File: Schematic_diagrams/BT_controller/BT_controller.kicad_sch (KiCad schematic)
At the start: 35 parts, among them J1 Conn_01x02_Socket, J1 Conn_2_Pin, J10 Conn_01x15_Socket, J11 Screw_Terminal_13-24_double_r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, J12 Screw_Terminal_58-60_double_r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, J13 Screw_Terminal_61-72_double_r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, J14 Screw_Terminal_3-4_partial_do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, J15 Conn_7_Pin, J2 D Sub Conn_9_Pin, J3 D Sub Conn_15_Pin, J4 Conn_01x07_Socket, J5 Conn_01x07_Socket, J5 Conn_7_Pin, J6 Screw_Terminal_13-24_double_r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, J7 Screw_Terminal_3-4_partial_do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, J8 Screw_Terminal_37-41_double_r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, J9 Screw_Terminal_1-2_partial_do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, SW1 ON/OFF, SW1 Start, SW3 SW_SPDT

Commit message: updates to rev B
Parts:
- added C2: 4700uF, symbol Device:C_Polarized
- added C3, C4: 0.1uF, symbol Device:C_Small
- added D2: SA12CA, symbol Device:D_TVS_Small_Filled
- added R2: 100R, symbol Device:R_Small
- BT_Bell_Push: value (none) -> SPST
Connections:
- net +10V: now also C2.1, C3.1, D2.2 (A2)
- net 8_Channel Relay Module #2/o/p8: now also R2.2
- net <- BT BELL SOUNDER (note 2): now also C4.1
- net GND: now also C2.2, C3.2, D2.1 (A1)
- net black: now also J10.14 (Pin_14), J8. (Pin_5)
- net black_twist: now also J10.2 (Pin_2), J7. (Pin_2)
- net blue: now also J10.12 (Pin_12), J8. (Pin_5)
- net brown: now also J10.15 (Pin_15), J8. (Pin_5)
- net orange: now also J10.8 (Pin_8), J6. (Pin_12)
- net violet: now also J10.13 (Pin_13), J8. (Pin_5)
- net white: now also J10.3 (Pin_3), J14. (Pin_2)
- net white_twist: now also J10.9 (Pin_9), J7. (Pin_2)
- net yellow: now also BT_Bell_Push.2, J10.4 (Pin_4)
- new net: C4.2, R2.1
- new net: J9.73 (Pin_1), J9.74 (Pin_2)
- now unconnected: J6.14 (Pin_2), J6.15 (Pin_3), J7.3 (Pin_1), J7.4 (Pin_2)
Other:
- note added: "1.4V"
- note added: "Trim pot for 5.0V"
- note removed: "10V"
- moved on the sheet: BT_Bell_Push

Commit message: further changes to rev B
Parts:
- added D6: 1N4005, Diode_THT:D_DO-41_SOD81_P10.16mm_Horizontal, symbol Diode:1N4005
- added D7: UF4007, Diode_THT:D_DO-201AD_P15.24mm_Horizontal, symbol Diode:UF5407
- BT_Bell_Push: value SPST -> SPST (spare contact)
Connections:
- net +10V: now also D7.1 (K)
- net GND: now also D7.2 (A)
- net at J1.1 (Pin_1): now also D6.2 (A); no longer SW1.. (B)
- new net: D6.1 (K), SW1.. (B)
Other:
- moved on the sheet: 270R, A1, A2, BT_Bell_Push, C3, F1, LM2596, SW1

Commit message: Amberley spelling corrected
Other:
- company: Amerley Museum - Billingshurst Signalbox -> Amberley Museum - Billingshurst Signalbox
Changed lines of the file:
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@@
 		(date "07/02/2026")
 		(rev "B")
-		(company "Amerley Museum - Billingshurst Signalbox")
+		(company "Amberley Museum - Billingshurst Signalbox")
 	)
 	(rectangle

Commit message: random number debug
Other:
- note added: "~{o/p ch1 MDD/MDF KE}"
- note added: "~{o/p ch1 Train Waiting KE}"
- note added: "~{o/p ch2 MDH(X) KE}"
- note added: "~{o/p ch2 UC KE}"
- note added: "~{o/p ch3 DA KE}"
- note added: "~{o/p ch3 UD KE}"
- note added: "~{o/p ch4 DB KE}"
- note added: "~{o/p ch4 UE KE}"
- note added: "~{o/p ch5 DC KE}"
- note added: "~{o/p ch5 UF KE}"
- note added: "~{o/p ch6 DD KE}"
- note added: "~{o/p ch6 MEK(X) KE}"
- note added: "~{o/p ch7 DE KE}"
- note added: "~{o/p ch7 MEL KE}"
- note added: "~{o/p ch8 BT Bell}"
- note removed: "o/p ch1 MDD/MDF KE"
- note removed: "o/p ch1 Train Waiting KE"
- note removed: "o/p ch2 MDH(X) KE"
- note removed: "o/p ch2 UC KE"
- note removed: "o/p ch3 DA KE"
- note removed: "o/p ch3 UD KE"
- note removed: "o/p ch4 DB KE"
- note removed: "o/p ch4 UE KE"
- note removed: "o/p ch5 DC KE"
- note removed: "o/p ch5 UF KE"
- note removed: "o/p ch6 DD KE"
- note removed: "o/p ch6 MEK(X) KE"
- note removed: "o/p ch7 DE KE"
- note removed: "o/p ch7 MEL KE"
- note removed: "o/p ch8 BT Bell"
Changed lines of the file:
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@@
 		)
 	)
-	(text "o/p ch1 Train Waiting KE"
+	(text "~{o/p ch1 Train Waiting KE}"
 		(exclude_from_sim no)
 		(at 175.1507 100.6578 0)
@@
 		)
 	)
-	(text "o/p ch1 MDD/MDF KE"
+	(text "~{o/p ch1 MDD/MDF KE}"
 		(exclude_from_sim no)
 		(at 175.5772 35.8317 0)
@@
 		)
 	)
-	(text "o/p ch5 DC KE"
+	(text "~{o/p ch5 DC KE}"
 		(exclude_from_sim no)
 		(at 172.72 45.72 0)
@@
 		)
 	)
-	(text "o/p ch3 DA KE"
+	(text "~{o/p ch3 DA KE}"
 		(exclude_from_sim no)
 		(at 172.6579 40.6238 0)
@@
 		)
 	)
-	(text "o/p ch5 UF KE"
+	(text "~{o/p ch5 UF KE}"
 		(exclude_from_sim no)
 		(at 171.4986 110.9344 0)
@@
 		)
 	)
-	(text "o/p ch4 UE KE"
+	(text "~{o/p ch4 UE KE}"
 		(exclude_from_sim no)
 		(at 171.442 108.4431 0)
@@
 		)
 	)
-	(text "o/p ch8 BT Bell"
+	(text "~{o/p ch8 BT Bell}"
 		(exclude_from_sim no)
 		(at 172.3715 118.4601 0)
@@
 		)
 	)
-	(text "o/p ch6 MEK(X) KE"
+	(text "~{o/p ch6 MEK(X) KE}"
 		(exclude_from_sim no)
 		(at 173.3105 113.454 0)
@@
 		)
 	)
-	(text "o/p ch4 DB KE"
+	(text "~{o/p ch4 DB KE}"
 		(exclude_from_sim no)
 		(at 172.729 43.1607 0)
@@
 		)
 	)
-	(text "o/p ch6 DD KE"
+	(text "~{o/p ch6 DD KE}"
 		(exclude_from_sim no)
 		(at 172.7733 48.2273 0)
@@
 		)
 	)
-	(text "o/p ch2 MDH(X) KE"
+	(text "~{o/p ch2 MDH(X) KE}"
 		(exclude_from_sim no)
 		(at 174.5612 38.3717 0)
@@
 		)
 	)
-	(text "o/p ch3 UD KE"
+	(text "~{o/p ch3 UD KE}"
 		(exclude_from_sim no)
 		(at 171.3571 105.8103 0)
@@
 		)
 	)
-	(text "o/p ch7 DE KE"
+	(text "~{o/p ch7 DE KE}"
 		(exclude_from_sim no)
 		(at 172.7378 50.7167 0)
@@
 		)
 	)
-	(text "o/p ch2 UC KE"
+	(text "~{o/p ch2 UC KE}"
 		(exclude_from_sim no)
 		(at 171.3288 103.2906 0)
@@
 		)
 	)
-	(text "o/p ch7 MEL KE"
+	(text "~{o/p ch7 MEL KE}"
 		(exclude_from_sim no)
 		(at 172.263 116.0586 0)

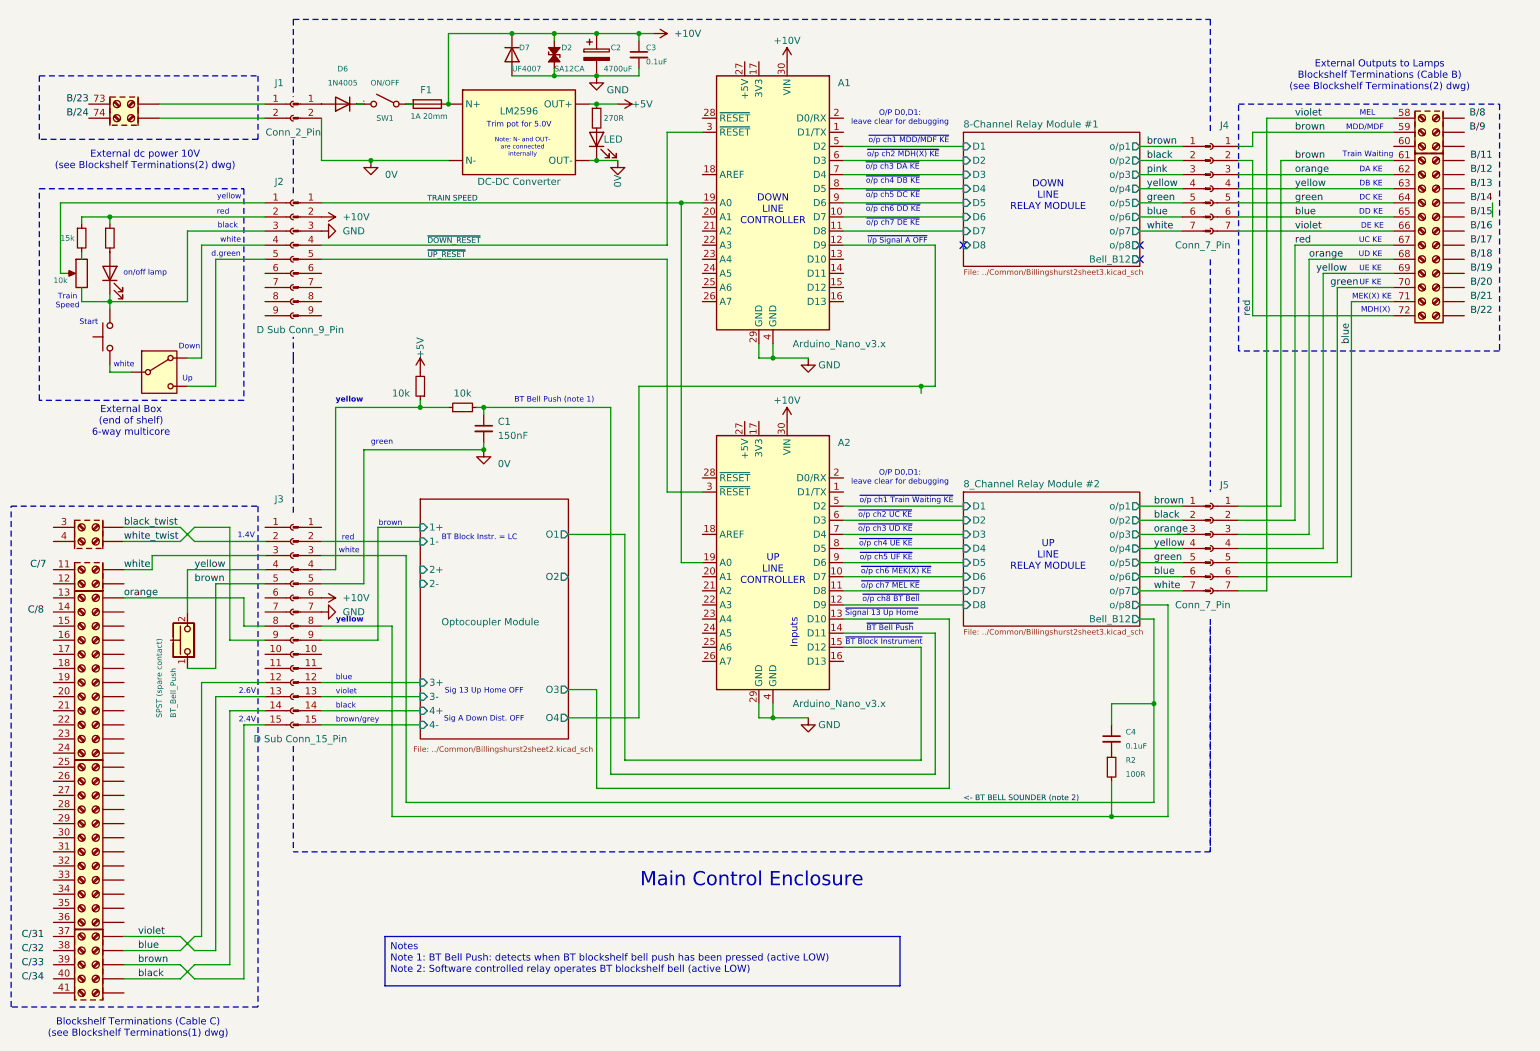
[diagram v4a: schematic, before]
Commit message: internal signal trial
trial was abandoned (inconsistent operation of interrupt)
though some changes were made to wiring and delays
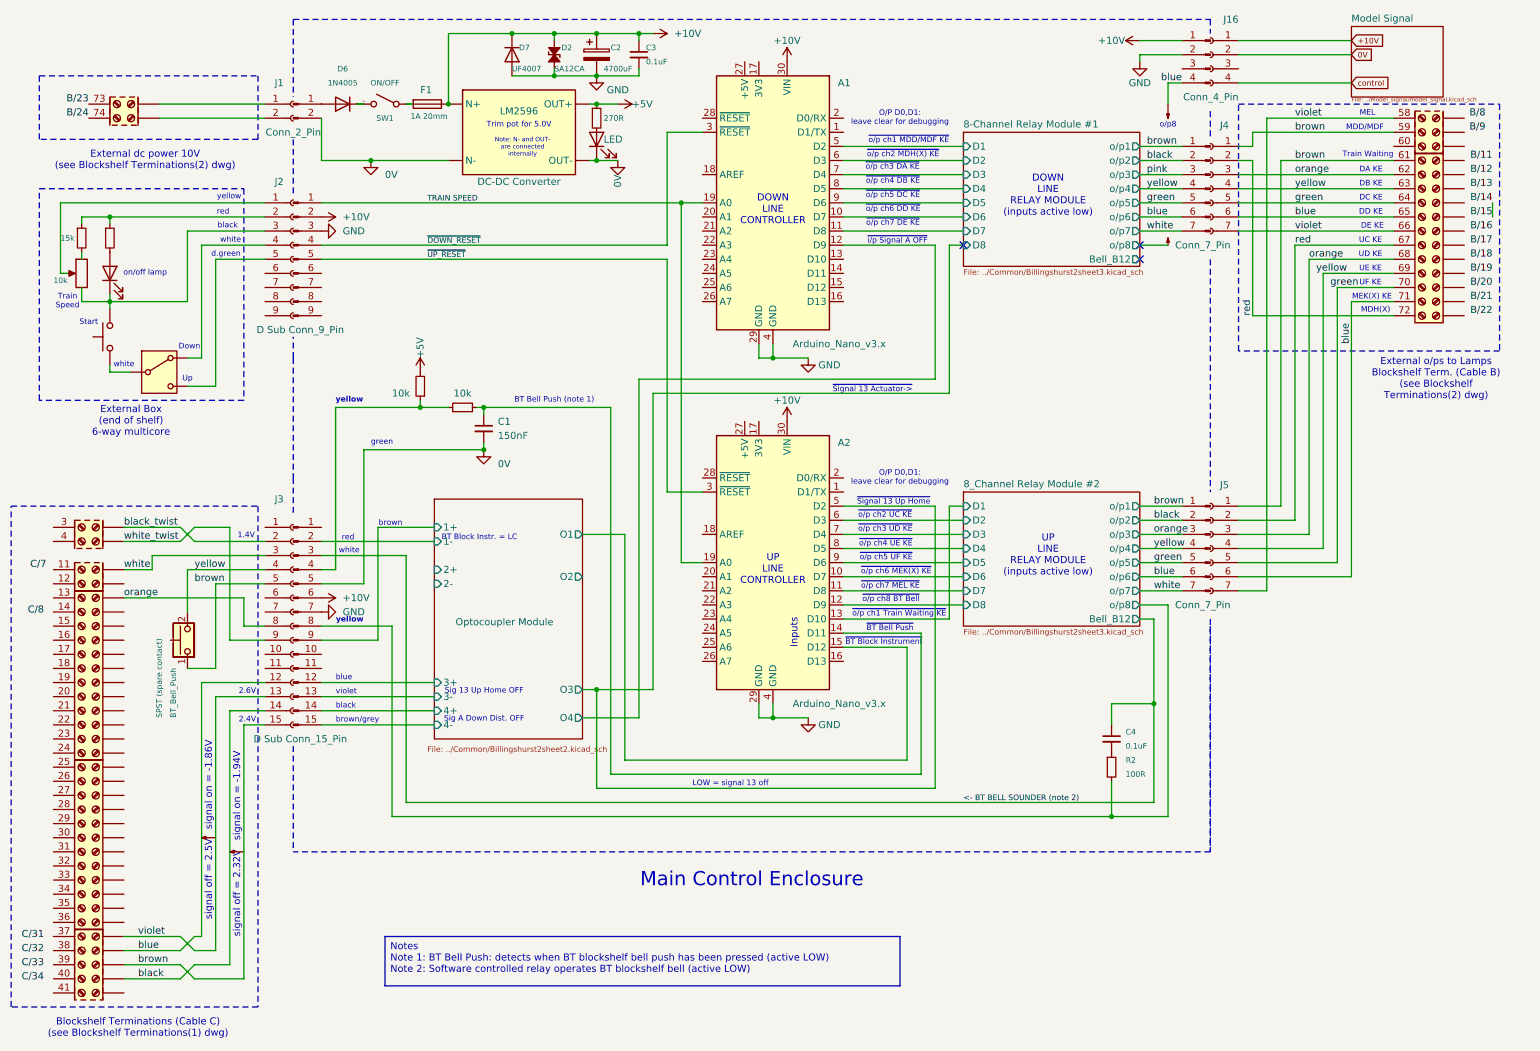
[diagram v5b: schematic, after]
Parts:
- added ?: ~, symbol Graphic:SYM_Arrow_Tiny
- added J16: Conn_4_Pin, symbol Connector:Conn_01x04_Socket
- added J17: Conn_4_Pin, symbol Connector:Conn_01x04_Pin
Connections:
- net Optocoupler Module/O3 is gone; now on net 8_Channel Relay Module #2/D1: A2.13 (D10)
- net +10V: now also J16.1 (Pin_1), J17.1 (Pin_1)
- net 8-Channel Relay Module #1/D8: now also A2.5 (D2)
- net 8_Channel Relay Module #2/D1: no longer A2.5 (D2)
- net GND: now also J17.2 (Pin_2)
- new net   0V : J16.2 (Pin_2)
- new net control: J16.4 (Pin_4)
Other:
- added sheet Model Signal (../Model_signal/model_signal.kicad_sch)
- note added: "DOWN LINE RELAY MODULE (inputs active low)"
- note added: "External o/ps to Lamps Blockshelf Term. (Cable B) (see Blockshelf Terminations(2) dwg)"
- note added: "LOW = signal 13 off"
- note added: "UP LINE RELAY MODULE (inputs active low)"
- note added: "o/p8"
- note added: "signal off = 2.32V signal on = -1.94V"
- note added: "signal off = 2.5V signal on = -1.86V"
- note added: "~{Signal 13 Actuator->}"
- note removed: "DOWN LINE RELAY MODULE"
- note removed: "External Outputs to Lamps Blockshelf Terminations (Cable B) (see Blockshelf Terminations(2) dwg)"
- note removed: "UP LINE RELAY MODULE"

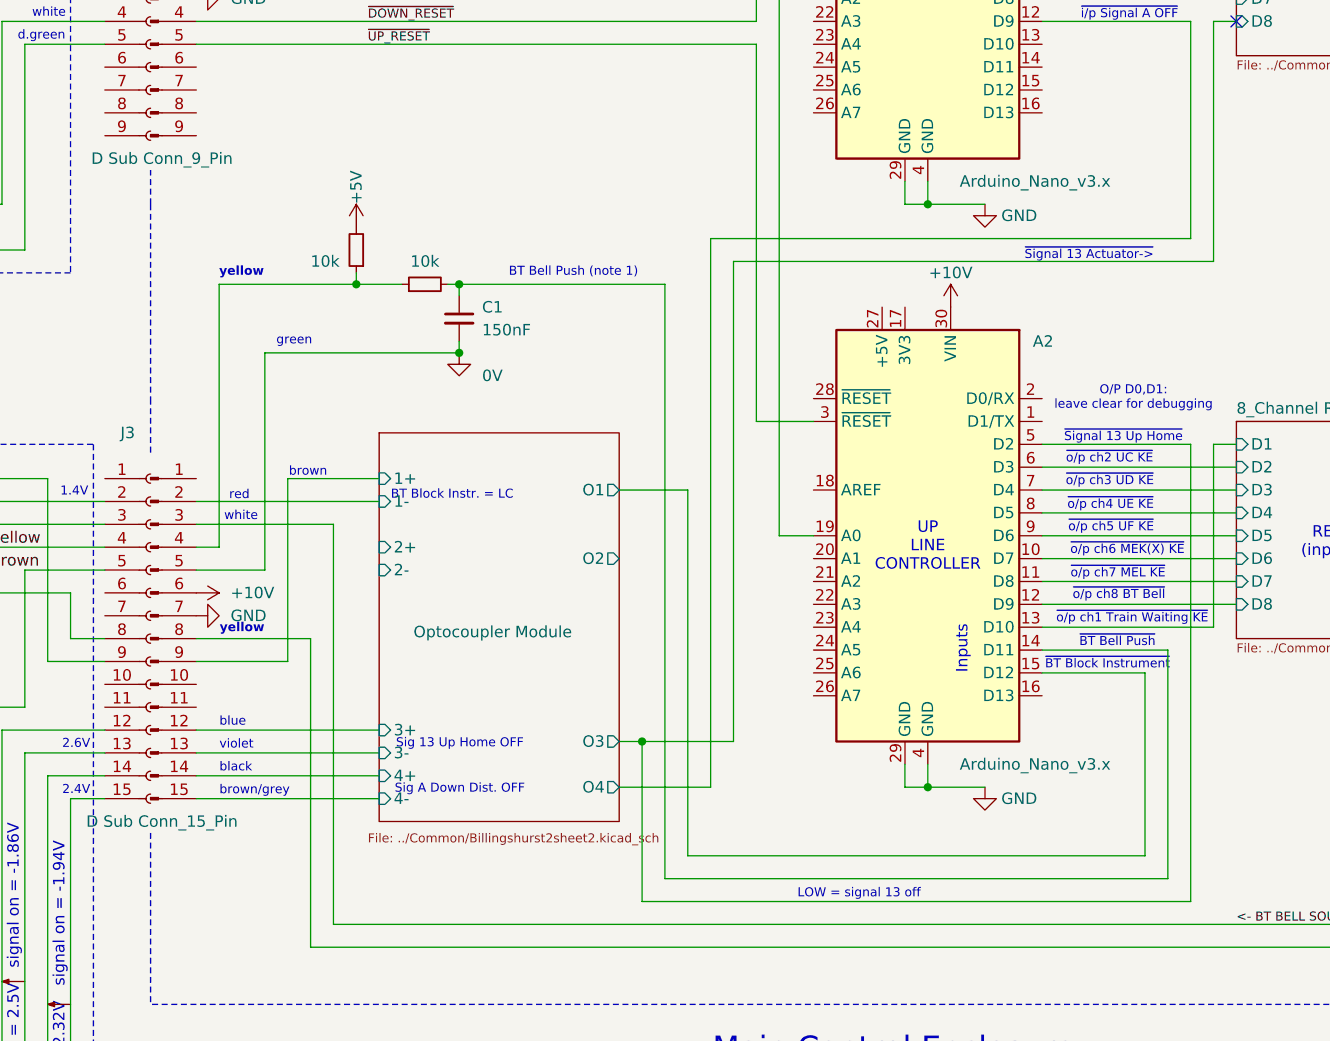
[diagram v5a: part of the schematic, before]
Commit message: low pass filter removed
low pass filter removed from BT bell press input - not required and possibly has connection issues
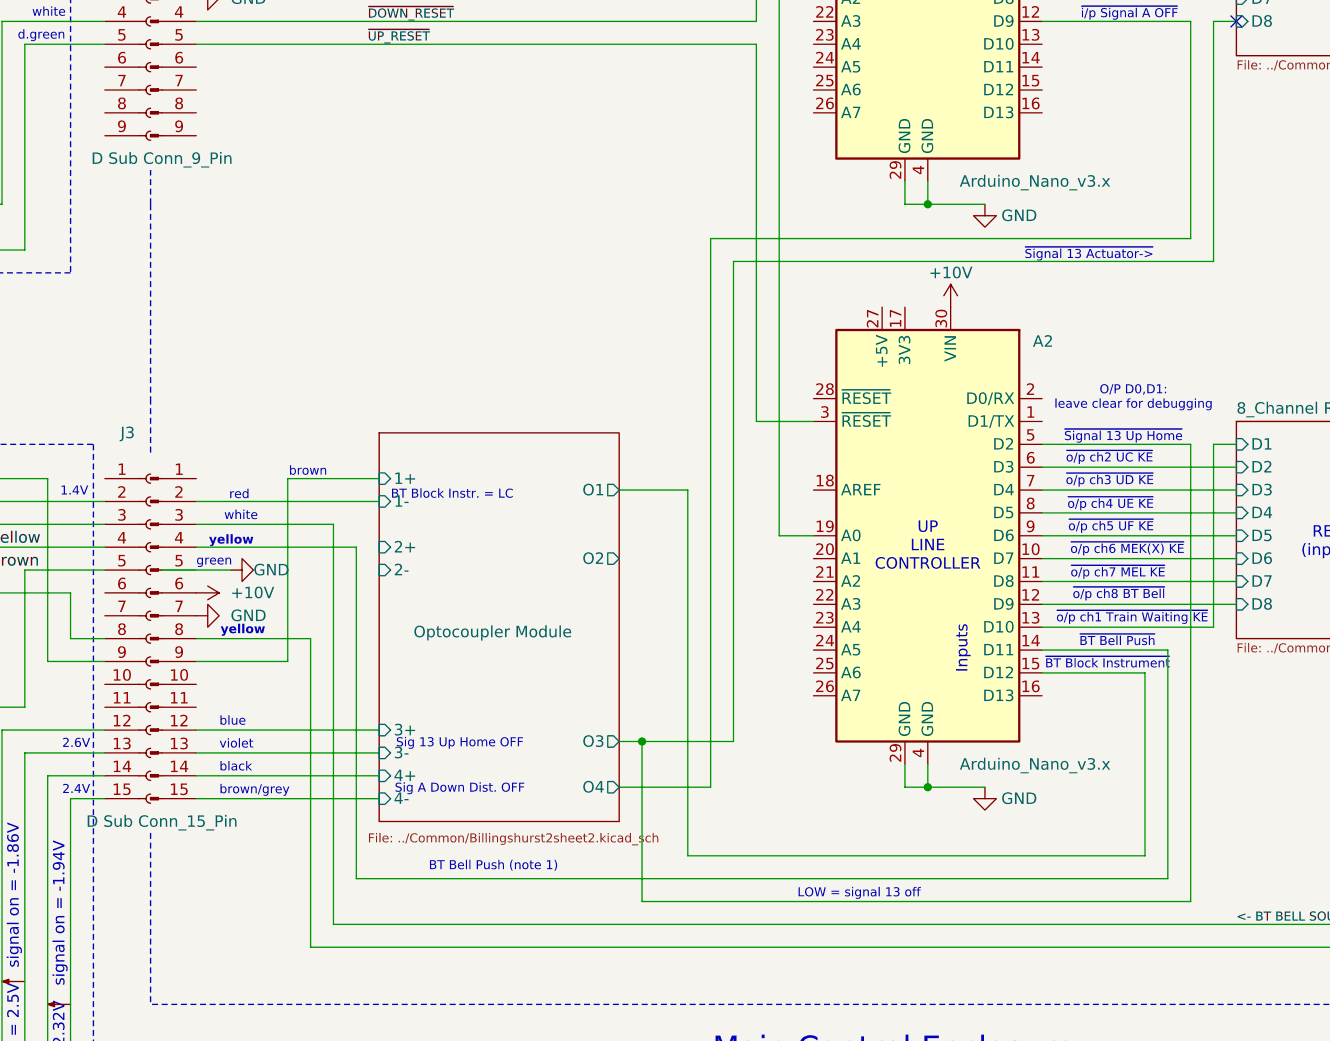
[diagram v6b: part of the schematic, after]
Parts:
- removed ? (x2): 10k, symbol Device:R_Small
- removed C1: 150nF, symbol Device:C_Small
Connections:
- net 0V: no longer J3.5 (Pin_5)
- net at A2.14 (D11): now also J3.4 (Pin_4)

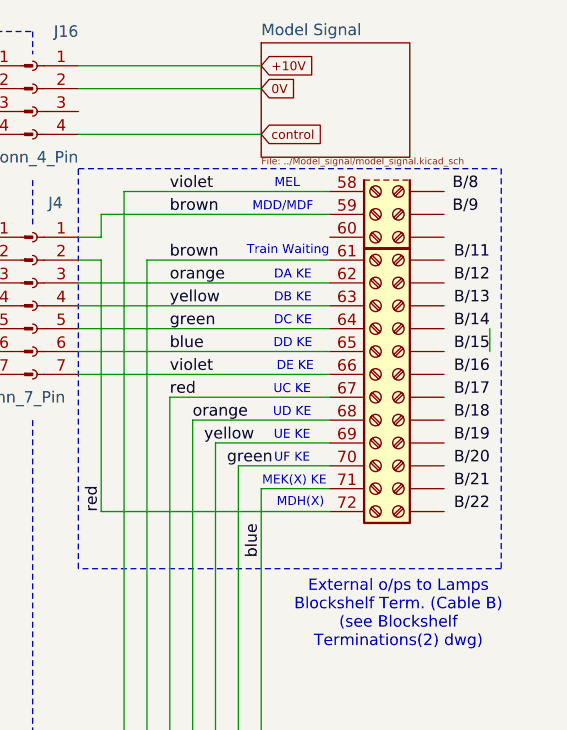
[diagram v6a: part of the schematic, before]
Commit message: controller schematic mod
label position
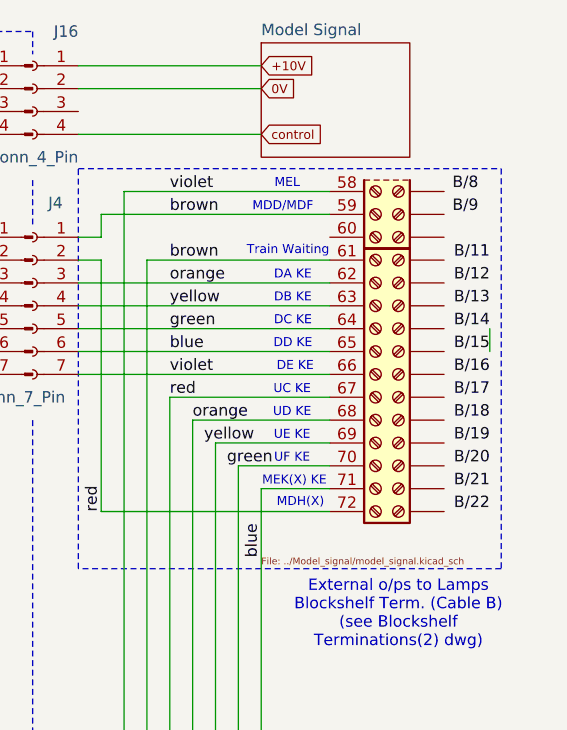
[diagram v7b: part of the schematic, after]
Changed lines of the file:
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@@
 		)
 		(property "Sheetfile" "../Model_signal/model_signal.kicad_sch"
-			(at 255.27 27.94 0)
+			(at 255.27 72.39 0)
 			(effects
 				(font

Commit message: Jim request
train held at second lamp until distant reversed
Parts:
- removed J11: Screw_Terminal_13-24_double_row, symbol Connector my_lib:Screw_Terminal_25-36_double_row
- removed J14, J7: Screw_Terminal_3-4_partial_double_row, symbol Connector my_lib:Screw_Terminal_3-4_partial_double_row
- added C1: 0.2uF, symbol Device:C_Small
- added J11: Screw_Terminal_13-24_double_row, symbol Connector my_lib:Screw_Terminal_13-24_double_row
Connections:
- net 8-Channel Relay Module #1/D8: no longer A2.5 (D2)
- net Optocoupler Module/2+: now also J3.10 (Pin_10)
- net Optocoupler Module/2-: now also J3.11 (Pin_11)
- net Optocoupler Module/O2: now also A2.5 (D2)
- net black_twist: no longer J10.2 (Pin_2)
- net brown: now also J10.5 (Pin_5), C1.2
- net white: now also J11. (Pin_12)
- net white_twist: no longer J10.9 (Pin_9)
- net yellow: now also C1.1; no longer BT_Bell_Push.2
- net at J10.10 (Pin_10): now also J11. (Pin_12)
- net at J10.11 (Pin_11): now also J11. (Pin_12)
- new net: J10.2 (Pin_2), J11. (Pin_12)
- new net: J10.9 (Pin_9), J11. (Pin_12)
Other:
- note added: "LOW = signal 14 off"
- note added: "Sig 14 Up Dist. OFF"
- note added: "~{Signal 14 Up Distant}"
- note removed: "LOW = signal 13 off"
- note removed: "~{Signal 13 Up Home}"
